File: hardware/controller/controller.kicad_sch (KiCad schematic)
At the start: 14 parts, among them J1 Conn_01x02_Pin, J2 Conn_01x02_Pin, J3 Conn_01x02_Pin, J4 Conn_01x02_Pin, J5 USB C Lipo Pins, J7 IMU (gnd/vdd side), J8 UWB, U1 ESP32-S3-DEVKITC-1-N8R8

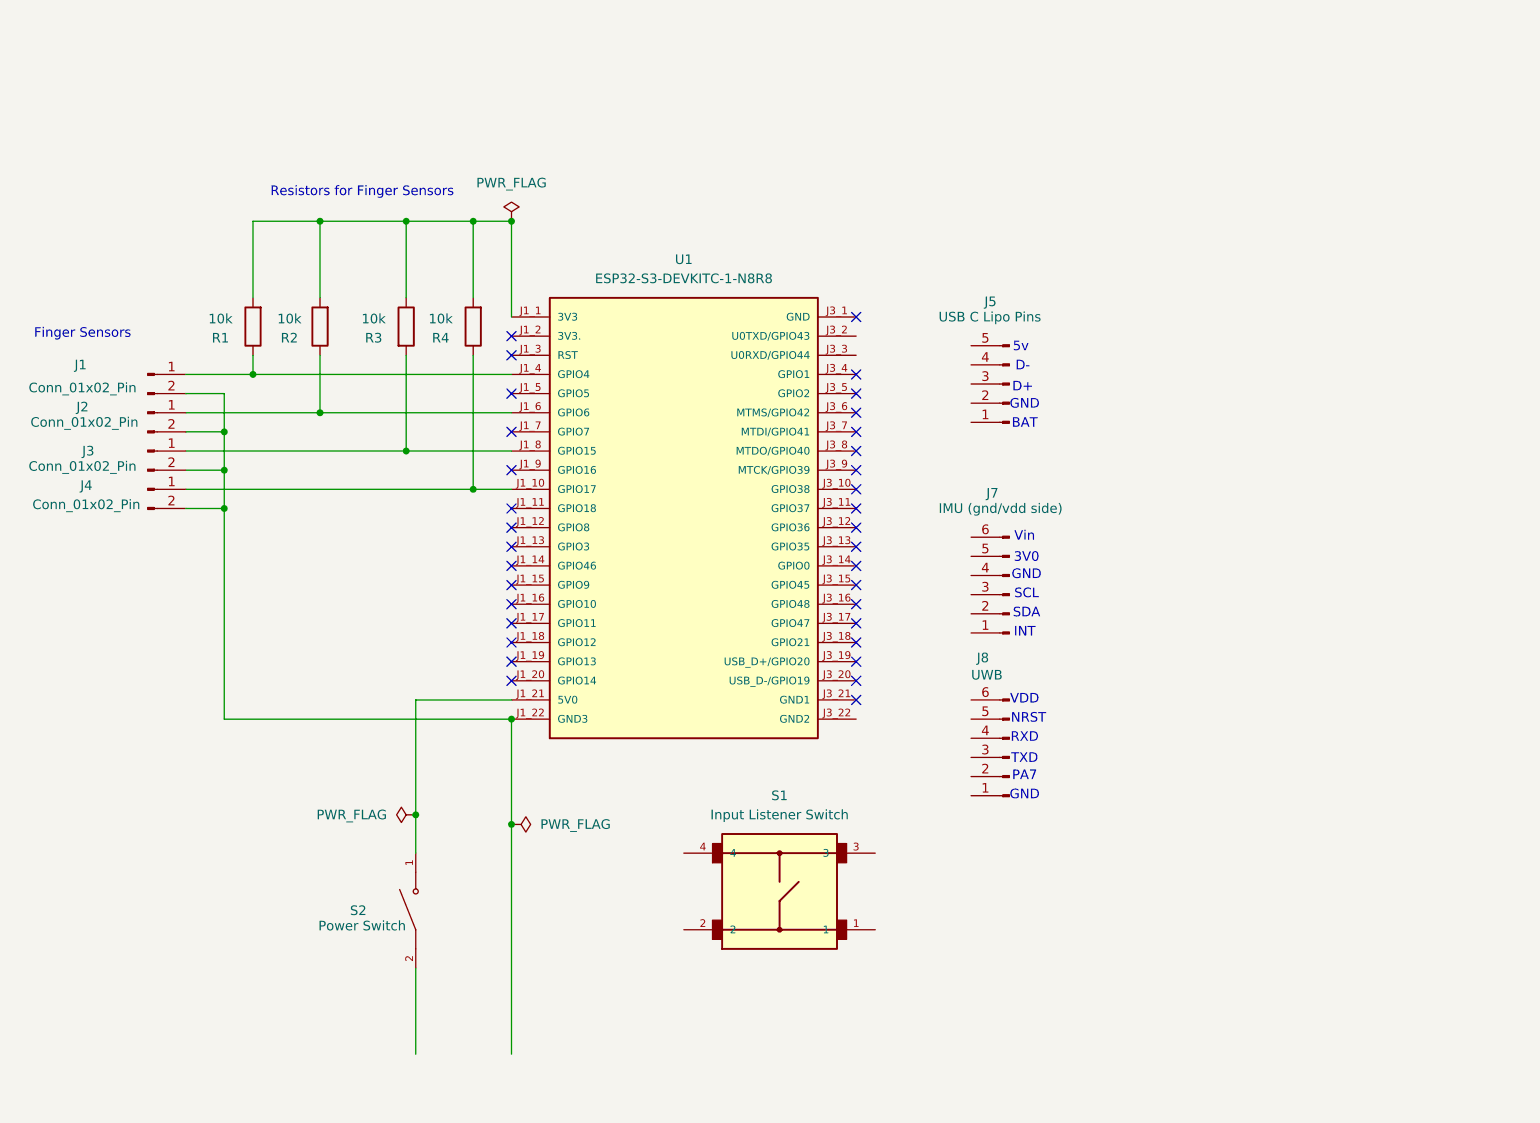
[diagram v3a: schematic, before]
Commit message: starting routing on schem
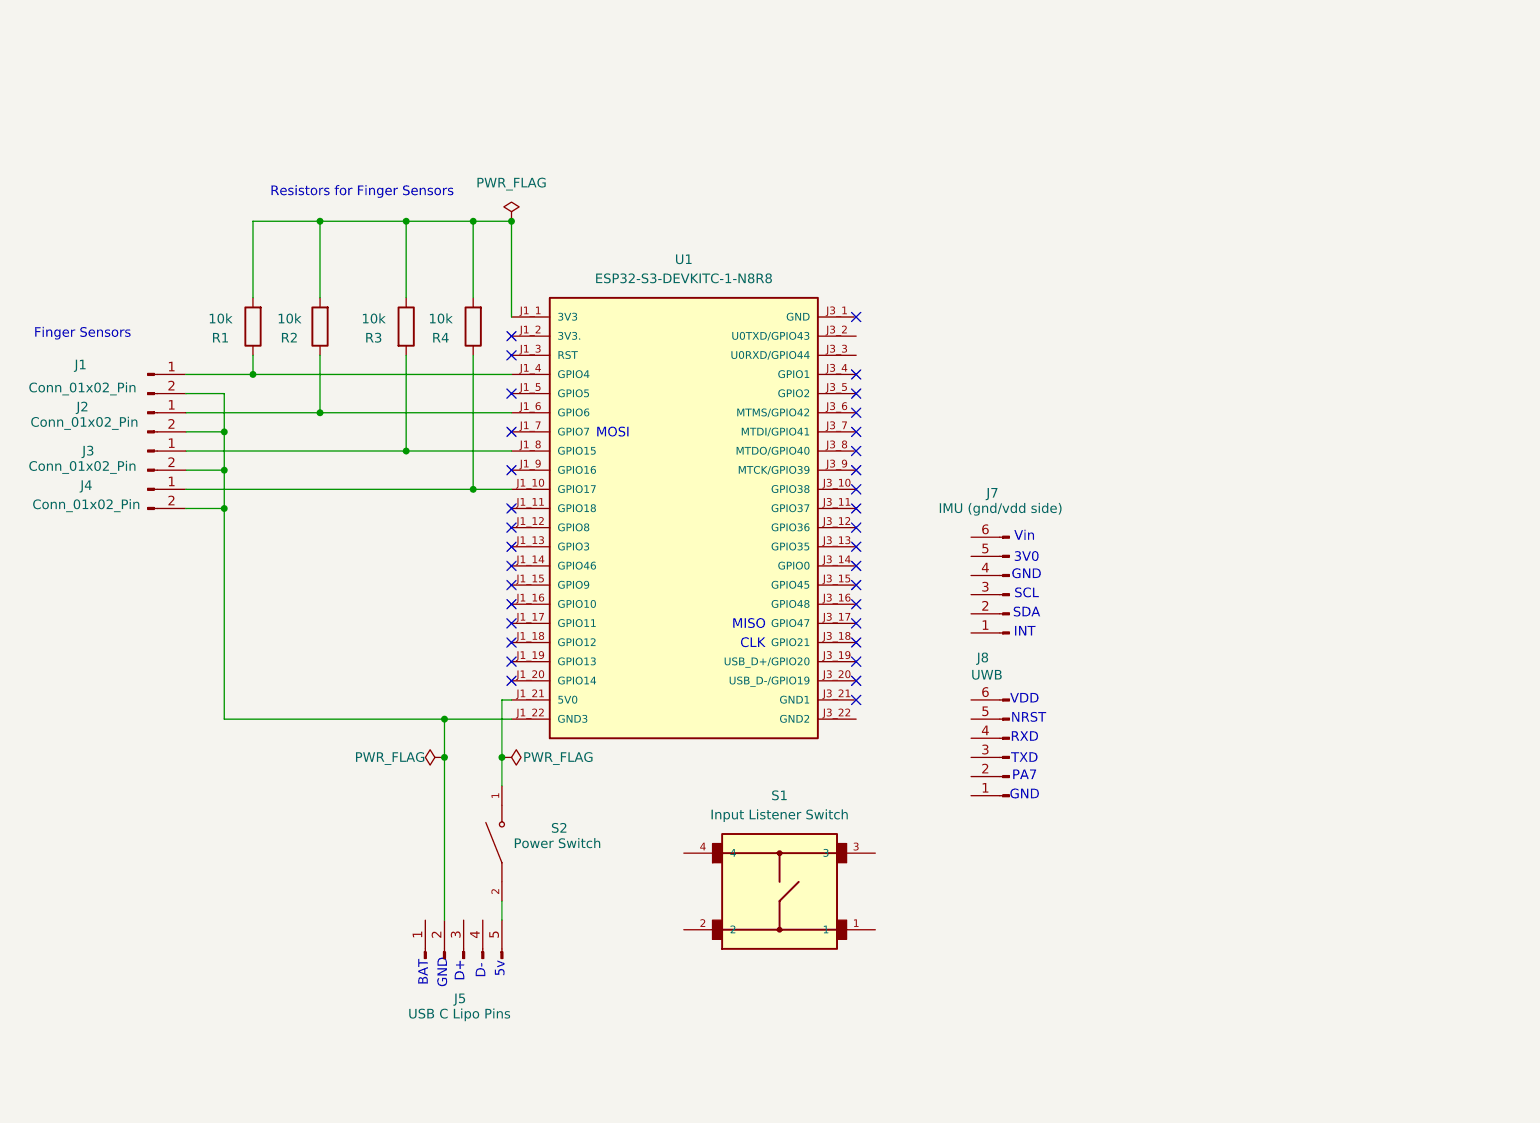
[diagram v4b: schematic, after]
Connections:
- net at J1.2 (Pin_2), J2.2 (Pin_2), J3.2 (Pin_2)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: now also J5.2 (Pin_2)
- net at S2.2: now also J5.5 (Pin_5)
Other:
- note added: "CLK"
- note added: "MISO"
- note added: "MOSI"
- moved on the sheet: J5, S2
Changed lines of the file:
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@@
+		)
+	)
+	(text "MISO"
+		(exclude_from_sim no)
+		(at 302.006 213.614 0)
+		(effects
+			(font
+				(size 1.27 1.27)
+			)
 		)
 	)
@@
 	(text "5v"
 		(exclude_from_sim no)
-		(at 338.074 176.784 0)
+		(at 268.986 259.334 90)
 		(effects
 			(font
@@
 	(text "BAT"
 		(exclude_from_sim no)
-		(at 338.582 186.944 0)
+		(at 258.826 259.842 90)
 		(effects
 			(font
@@
 	(text "D-"
 		(exclude_from_sim no)
-		(at 338.328 179.324 0)
+		(at 266.446 259.588 90)
 		(effects
 			(font
@@
 	(text "GND"
 		(exclude_from_sim no)
-		(at 338.582 184.404 0)
+		(at 261.366 259.842 90)
 		(effects
 			(font
@@
 	(text "D+"
 		(exclude_from_sim no)
-		(at 338.328 182.118 0)
+		(at 263.652 259.588 90)
+		(effects
+			(font
+				(size 1.27 1.27)
+			)
+		)
+	)
+	(text "MOSI"
+		(exclude_from_sim no)
+		(at 283.972 188.214 0)
 		(effects
 			(font
@@
 		)
 	)
+	(text "CLK"
+		(exclude_from_sim no)
+		(at 302.514 216.154 0)
+		(effects
+			(font
+				(size 1.27 1.27)
+			)
+		)
+	)
 	(text "Finger Sensors"
 		(exclude_from_sim no)
@@
 	)
 	(junction
-		(at 270.51 240.03)
+		(at 261.62 231.14)
 		(diameter 0)
 		(color 0 0 0 0)
 	)
 	(junction
-		(at 270.51 226.06)
+		(at 261.62 226.06)
 		(diameter 0)
 		(color 0 0 0 0)
@@
 	)
 	(junction
-		(at 257.81 238.76)
+		(at 269.24 231.14)
 		(diameter 0)
 		(color 0 0 0 0)
@@
 	(wire
 		(pts
+			(xy 261.62 226.06) (xy 270.51 226.06)
+		)
+		(stroke
+			(width 0)
+			(type default)
+		)
+	)
+	(wire
+		(pts
 			(xy 232.41 187.96) (xy 232.41 193.04)
 		)
@@
 	(wire
 		(pts
-			(xy 257.81 259.08) (xy 257.81 270.51)
+			(xy 269.24 250.19) (xy 269.24 252.73)
 		)
 		(stroke
@@
 	(wire
 		(pts
-			(xy 257.81 243.84) (xy 257.81 238.76)
-		)
-		(stroke
-			(width 0)
-			(type default)
-		)
-	)
-	(wire
-		(pts
-			(xy 257.81 238.76) (xy 257.81 223.52)
-		)
-		(stroke
-			(width 0)
-			(type default)
-		)
-	)
-	(wire
-		(pts
-			(xy 257.81 223.52) (xy 270.51 223.52)
-		)
-		(stroke
-			(width 0)
-			(type default)
-		)
-	)
-	(wire
-		(pts
-			(xy 232.41 226.06) (xy 270.51 226.06)
+			(xy 269.24 223.52) (xy 269.24 231.14)
+		)
+		(stroke
+			(width 0)
+			(type default)
+		)
+	)
+	(wire
+		(pts
+			(xy 269.24 223.52) (xy 270.51 223.52)
+		)
+		(stroke
+			(width 0)
+			(type default)
+		)
+	)
+	(wire
+		(pts
+			(xy 232.41 226.06) (xy 261.62 226.06)
 		)
 		(stroke
@@
 	(wire
 		(pts
+			(xy 261.62 231.14) (xy 261.62 252.73)
+		)
+		(stroke
+			(width 0)
+			(type default)
+		)
+	)
+	(wire
+		(pts
 			(xy 232.41 193.04) (xy 232.41 198.12)
 		)
@@
 	(wire
 		(pts
-			(xy 270.51 270.51) (xy 270.51 240.03)
-		)
-		(stroke
-			(width 0)
-			(type default)
-		)
-	)
-	(wire
-		(pts
 			(xy 256.54 160.02) (xy 256.54 170.18)
 		)
@@
 	(wire
 		(pts
-			(xy 270.51 240.03) (xy 270.51 226.06)
+			(xy 261.62 226.06) (xy 261.62 231.14)
 		)
 		(stroke
@@
 		(pts
 			(xy 227.33 190.5) (xy 256.54 190.5)
+		)
+		(stroke
+			(width 0)
+			(type default)
+		)
+	)
+	(wire
+		(pts
+			(xy 269.24 231.14) (xy 269.24 234.95)
 		)
 		(stroke
@@
 	(symbol
 		(lib_id "power:PWR_FLAG")
-		(at 270.51 240.03 270)
+		(at 261.62 231.14 90)
 		(unit 1)
 		(exclude_from_sim no)
@@
 		(on_board yes)
 		(dnp no)
-		(fields_autoplaced yes)
 		(property "Reference" "#FLG02"
-			(at 272.415 240.03 0)
+			(at 259.715 231.14 0)
 			(effects
 				(font
@@
 		)
 		(property "Value" "PWR_FLAG"
-			(at 274.32 240.0299 90)
+			(at 259.08 231.14 90)
 			(effects
 				(font
@@
 		)
 		(property "Footprint" ""
-			(at 270.51 240.03 0)
+			(at 261.62 231.14 0)
 			(effects
 				(font
@@
 		)
 		(property "Datasheet" "~"
-			(at 270.51 240.03 0)
+			(at 261.62 231.14 0)
 			(effects
 				(font
@@
 		)
 		(property "Description" "Special symbol for telling ERC where power comes from"
-			(at 270.51 240.03 0)
+			(at 261.62 231.14 0)
 			(effects
 				(font
@@
 	(symbol
 		(lib_id "GF-123-0054:GF-123-0054")
-		(at 257.81 251.46 90)
+		(at 269.24 242.57 90)
 		(unit 1)
 		(exclude_from_sim no)
@@
 		(dnp no)
 		(property "Reference" "S2"
-			(at 250.19 251.46 90)
+			(at 276.86 240.538 90)
 			(effects
 				(font
@@
 		)
 		(property "Value" "Power Switch"
-			(at 250.698 253.492 90)
+			(at 276.606 242.57 90)
 			(effects
 				(font
@@
 		)
 		(property "Footprint" "GF-123-0054:SW_GF-123-0054"
-			(at 257.81 251.46 0)
+			(at 269.24 242.57 0)
 			(effects
 				(font
@@
 		)
 		(property "Datasheet" ""
-			(at 257.81 251.46 0)
+			(at 269.24 242.57 0)
 			(effects
 				(font
@@
 		)
 		(property "Description" ""
-			(at 257.81 251.46 0)
+			(at 269.24 242.57 0)
 			(effects
 				(font
@@
 		)
 		(property "PARTREV" "May 20, 2003"
-			(at 257.81 251.46 0)
+			(at 269.24 242.57 0)
 			(effects
 				(font
@@
 		)
 		(property "MANUFACTURER" "CW Industries"
-			(at 257.81 251.46 0)
+			(at 269.24 242.57 0)
 			(effects
 				(font
@@
 		)
 		(property "MAXIMUM_PACKAGE_HIEGHT" "14.96 mm"
-			(at 257.81 251.46 0)
+			(at 269.24 242.57 0)
 			(effects
 				(font
@@
 		)
 		(property "STANDARD" "Manufacturer Recommendations"
-			(at 257.81 251.46 0)
+			(at 269.24 242.57 0)
 			(effects
 				(font
@@
 	(symbol
 		(lib_id "power:PWR_FLAG")
-		(at 257.81 238.76 90)
+		(at 269.24 231.14 270)
 		(unit 1)
 		(exclude_from_sim no)
@@
 		(on_board yes)
 		(dnp no)
-		(fields_autoplaced yes)
 		(property "Reference" "#FLG01"
-			(at 255.905 238.76 0)
+			(at 271.145 231.14 0)
 			(effects
 				(font
@@
 		)
 		(property "Value" "PWR_FLAG"
-			(at 254 238.7599 90)
+			(at 272.034 231.14 90)
 			(effects
 				(font
@@
 		)
 		(property "Footprint" ""
-			(at 257.81 238.76 0)
+			(at 269.24 231.14 0)
 			(effects
 				(font
@@
 		)
 		(property "Datasheet" "~"
-			(at 257.81 238.76 0)
+			(at 269.24 231.14 0)
 			(effects
 				(font
@@
 		)
 		(property "Description" "Special symbol for telling ERC where power comes from"
-			(at 257.81 238.76 0)
+			(at 269.24 231.14 0)
 			(effects
 				(font
@@
 	(symbol
 		(lib_id "Connector:Conn_01x05_Pin")
-		(at 336.55 181.61 180)
+		(at 264.16 257.81 90)
 		(unit 1)
 		(exclude_from_sim no)
@@
 		(dnp no)
 		(property "Reference" "J5"
-			(at 333.248 170.688 0)
+			(at 262.89 263.144 90)
 			(effects
 				(font
@@
 		)
 		(property "Value" "USB C Lipo Pins"
-			(at 327.152 172.72 0)
+			(at 256.794 265.176 90)
 			(effects
 				(font
@@
 		)
 		(property "Footprint" ""
-			(at 336.55 181.61 0)
+			(at 264.16 257.81 0)
 			(effects
 				(font
@@
 		)
 		(property "Datasheet" "~"
-			(at 336.55 181.61 0)
+			(at 264.16 257.81 0)
 			(effects
 				(font
@@
 		)
 		(property "Description" "Generic connector, single row, 01x05, script generated"
-			(at 336.55 181.61 0)
-			(effects
-				(font
+			(at 264.16 257.81 0)
+			(effects
+				(font

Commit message: schem wiring should be done
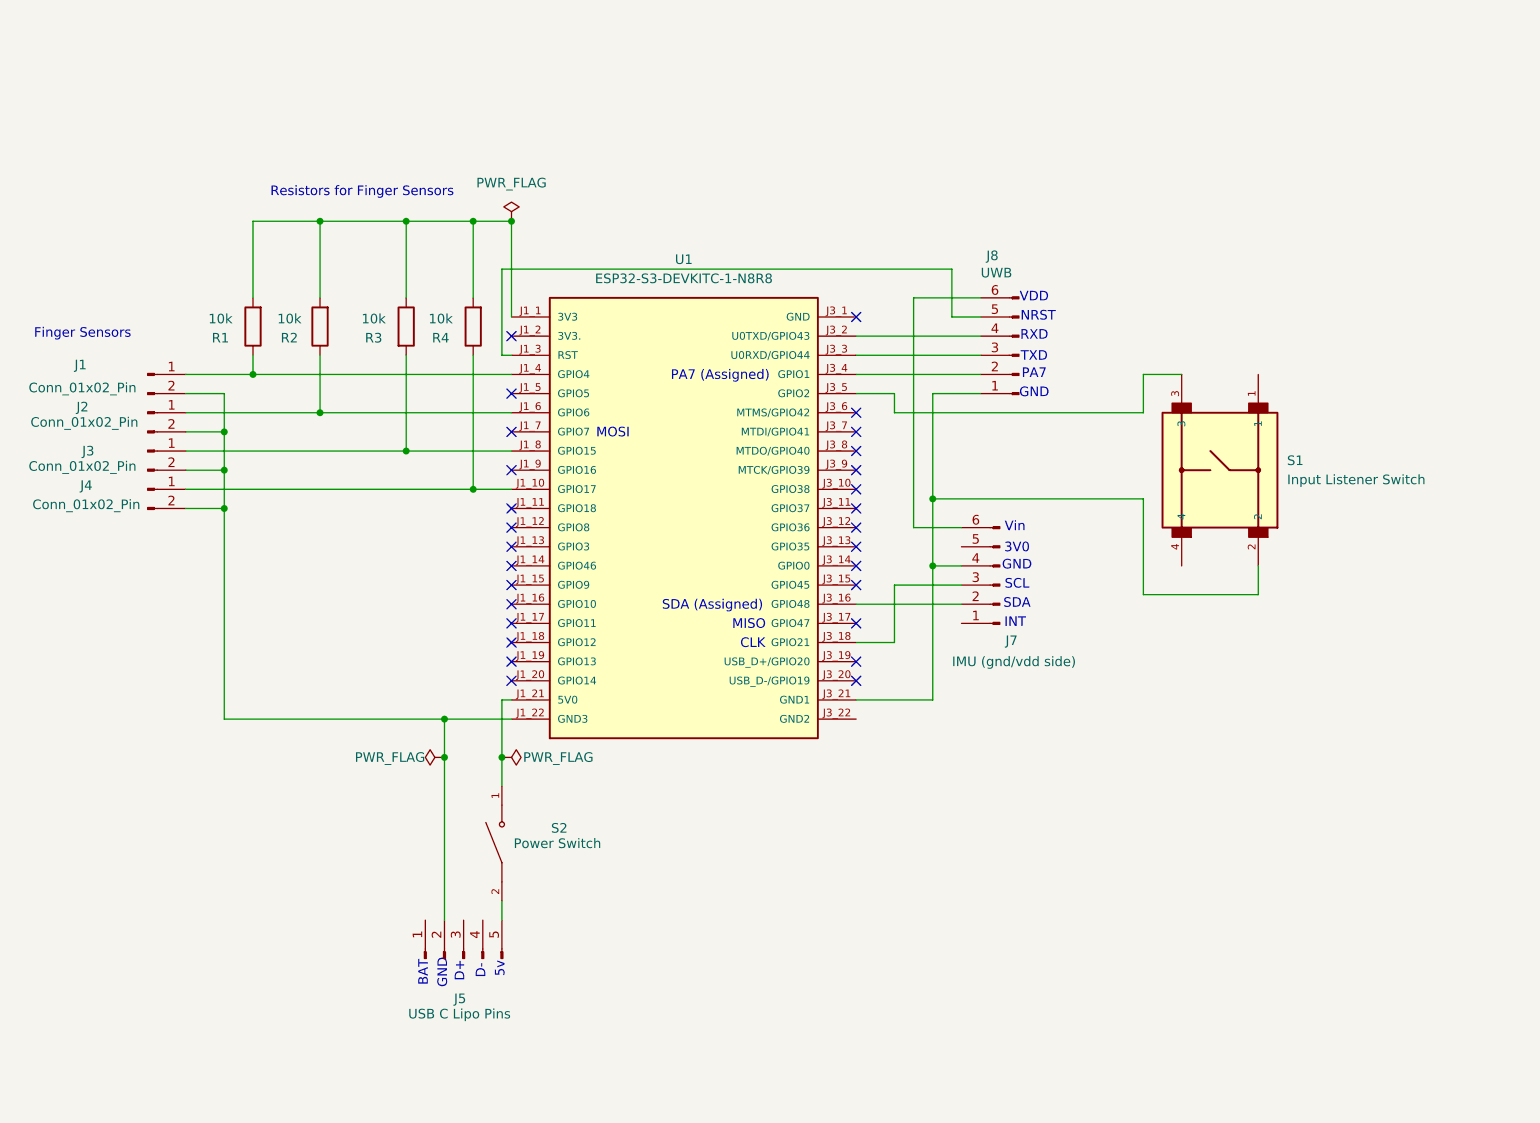
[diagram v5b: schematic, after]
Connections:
- net at U1.J1_3 (RST): now also J8.5 (Pin_5)
- net at U1.J3_16 (GPIO48): now also J7.2 (Pin_2)
- net at U1.J3_18 (GPIO21): now also J7.3 (Pin_3)
- net at U1.J3_2 (U0TXD/GPIO43): now also J8.4 (Pin_4)
- net at U1.J3_21 (GND1): now also J7.4 (Pin_4), J8.1 (Pin_1), S1.2
- net at U1.J3_3 (U0RXD/GPIO44): now also J8.3 (Pin_3)
- net at U1.J3_4 (GPIO1): now also J8.2 (Pin_2)
- net at U1.J3_5 (GPIO2): now also S1.3
- net at J7.6 (Pin_6): now also J8.6 (Pin_6)
- no-connect marks 34 -> 28
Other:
- note added: "PA7 (Assigned)"
- note added: "SDA (Assigned)"
- moved on the sheet: J7, J8, S1

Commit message: some ERC resolved, checkpoint
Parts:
- J5: footprint (none) -> Connector_PinSocket_2.54mm:PinSocket_1x05_P2.54mm_Vertical
- J7, J8: footprint (none) -> Connector_PinSocket_2.54mm:PinSocket_1x06_P2.54mm_Vertical
- S1: value Input Listener Switch -> B3F-1000
- S2: value Power Switch -> GF-123-0054
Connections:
- no-connect marks 28 -> 36
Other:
- note added: "Event Listener Switch"
- note added: "Power Switch"
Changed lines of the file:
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@@
+		)
+	)
+	(text "Power Switch"
+		(exclude_from_sim no)
+		(at 278.384 256.54 0)
+		(effects
+			(font
+				(size 1.27 1.27)
+			)
 		)
 	)
@@
 		)
 	)
+	(text "Event Listener Switch"
+		(exclude_from_sim no)
+		(at 392.176 189.484 0)
+		(effects
+			(font
+				(size 1.27 1.27)
+			)
+		)
+	)
 	(text "SDA (Assigned)"
 		(exclude_from_sim no)
@@
 	)
 	(junction
+		(at 325.12 223.52)
+		(diameter 0)
+		(color 0 0 0 0)
+	)
+	(junction
 		(at 236.22 180.34)
 		(diameter 0)
@@
 	)
 	(no_connect
+		(at 266.7 252.73)
+	)
+	(no_connect
 		(at 270.51 215.9)
 	)
 	(no_connect
+		(at 330.2 203.2)
+	)
+	(no_connect
 		(at 316.23 203.2)
 	)
@@
 	)
 	(no_connect
+		(at 359.41 205.74)
+	)
+	(no_connect
 		(at 316.23 187.96)
 	)
@@
 	)
 	(no_connect
+		(at 330.2 213.36)
+	)
+	(no_connect
 		(at 316.23 198.12)
 	)
 	(no_connect
+		(at 316.23 226.06)
+	)
+	(no_connect
 		(at 316.23 190.5)
 	)
@@
 	)
 	(no_connect
+		(at 369.57 180.34)
+	)
+	(no_connect
+		(at 264.16 252.73)
+	)
+	(no_connect
 		(at 270.51 213.36)
 	)
@@
 	)
 	(no_connect
+		(at 259.08 252.73)
+	)
+	(no_connect
 		(at 270.51 208.28)
 	)
@@
 	(wire
 		(pts
-			(xy 316.23 223.52) (xy 326.39 223.52)
+			(xy 316.23 223.52) (xy 325.12 223.52)
 		)
 		(stroke
@@
 		(pts
 			(xy 328.93 172.72) (xy 332.74 172.72)
+		)
+		(stroke
+			(width 0)
+			(type default)
+		)
+	)
+	(wire
+		(pts
+			(xy 325.12 223.52) (xy 326.39 223.52)
 		)
 		(stroke
@@
 			)
 		)
-		(property "Footprint" ""
+		(property "Footprint" "Connector_PinSocket_2.54mm:PinSocket_1x06_P2.54mm_Vertical"
 			(at 335.28 208.28 0)
 			(effects
@@
 			)
 		)
-		(property "Footprint" ""
+		(property "Footprint" "Connector_PinSocket_2.54mm:PinSocket_1x06_P2.54mm_Vertical"
 			(at 337.82 177.8 0)
 			(effects
@@
 	)
 	(symbol
+		(lib_id "power:PWR_FLAG")
+		(at 325.12 223.52 180)
+		(unit 1)
+		(exclude_from_sim no)
+		(in_bom yes)
+		(on_board yes)
+		(dnp no)
+		(fields_autoplaced yes)
+		(property "Reference" "#FLG03"
+			(at 325.12 225.425 0)
+			(effects
+				(font
+					(size 1.27 1.27)
+				)
+				(hide yes)
+			)
+		)
+		(property "Value" "PWR_FLAG"
+			(at 325.12 228.6 0)
+			(effects
+				(font
+					(size 1.27 1.27)
+				)
+			)
+		)
+		(property "Footprint" ""
+			(at 325.12 223.52 0)
+			(effects
+				(font
+					(size 1.27 1.27)
+				)
+				(hide yes)
+			)
+		)
+		(property "Datasheet" "~"
+			(at 325.12 223.52 0)
+			(effects
+				(font
+					(size 1.27 1.27)
+				)
+				(hide yes)
+			)
+		)
+		(property "Description" "Special symbol for telling ERC where power comes from"
+			(at 325.12 223.52 0)
+			(effects
+				(font
+					(size 1.27 1.27)
+				)
+				(hide yes)
+			)
+		)
+		(pin "1"
+		)
+		(instances
+			(project ""
+				(path "/50de191a-06b5-4968-8f0c-17f7744c4812"
+					(reference "#FLG03")
+					(unit 1)
+				)
+			)
+		)
+	)
+	(symbol
 		(lib_id "GF-123-0054:GF-123-0054")
 		(at 269.24 242.57 90)
@@
 			)
 		)
-		(property "Value" "Power Switch"
-			(at 276.606 242.57 90)
+		(property "Value" "GF-123-0054"
+			(at 278.13 242.316 90)
 			(effects
 				(font
@@
 			)
 		)
-		(property "Value" "Input Listener Switch"
+		(property "Value" "B3F-1000"
 			(at 373.38 194.3114 90)
 			(effects
@@
 			)
 		)
-		(property "Footprint" ""
+		(property "Footprint" "Connector_PinSocket_2.54mm:PinSocket_1x05_P2.54mm_Vertical"
 			(at 264.16 257.81 0)
 			(effects

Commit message: schematic ERC passed
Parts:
- S1: footprint B3F-1000:SW_B3F-1000 -> B3F_1000:SW_B3F-1000
- S2: footprint GF-123-0054:SW_GF-123-0054 -> GF_123_0054:SW_GF-123-0054
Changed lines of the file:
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@@
 			)
 		)
-		(property "Footprint" "GF-123-0054:SW_GF-123-0054"
+		(property "Footprint" "GF_123_0054:SW_GF-123-0054"
 			(at 269.24 242.57 0)
 			(effects
@@
 			)
 		)
-		(property "Footprint" "B3F-1000:SW_B3F-1000"
+		(property "Footprint" "B3F_1000:SW_B3F-1000"
 			(at 364.49 193.04 0)
 			(effects
